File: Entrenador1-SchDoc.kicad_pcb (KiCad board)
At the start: 2 copper layers, 152.4 x 106.7 mm, 88 parts, among them CON1 BARREL_JACK, J11 CON8, J3 ICSP, J5 CON8, J6 CON8, J7 CON8, J9 3vias, P1 CONN_01X04, P10 CONN_01X04, P2 CONN_01X04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

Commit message: adición del BOM
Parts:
- C10, C9: value C -> 22pf
- C11: value CP -> 1uf
- C6: value ~ -> 10uf
- C7: value C -> 100nf
- C8: value CP -> 47uf
- D12: value D -> 1n4004
- RV1, RV2: value POT -> 10K lin
- Y2: value XTAL -> 20MHz
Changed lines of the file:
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@@
   (general
     (links 239)
-    (no_connects 0)
-    (area 65.989999 32.969999 218.490001 139.750001)
+    (no_connects 13)
+    (area 64.616667 32.969999 230.290572 149.258)
     (thickness 1.6)
     (drawings 118)
@@
       (effects (font (size 1 1) (thickness 0.15)))
     )
-    (fp_text value C (at 1.25 2.56) (layer F.Fab)
+    (fp_text value 22pf (at 1.25 2.56) (layer F.Fab)
       (effects (font (size 1 1) (thickness 0.15)))
     )
@@
       (effects (font (size 1 1) (thickness 0.15)))
     )
-    (fp_text value C (at 1.25 2.56 180) (layer F.Fab)
+    (fp_text value 22pf (at 1.25 2.56 180) (layer F.Fab)
       (effects (font (size 1 1) (thickness 0.15)))
     )
@@
       (effects (font (size 1 1) (thickness 0.15)))
     )
-    (fp_text value C (at 1.25 2.56 180) (layer F.Fab)
+    (fp_text value 100nf (at 1.25 2.56 180) (layer F.Fab)
       (effects (font (size 1 1) (thickness 0.15)))
     )
@@
       (effects (font (size 1 1) (thickness 0.15)))
     )
-    (fp_text value CP (at 1.25 3.81 180) (layer F.Fab)
+    (fp_text value 1uf (at 1.25 3.81 180) (layer F.Fab)
       (effects (font (size 1 1) (thickness 0.15)))
     )
@@
       (effects (font (size 1 1) (thickness 0.15)))
     )
-    (fp_text value CP (at 1.25 3.81 270) (layer F.Fab)
+    (fp_text value 47uf (at 1.25 3.81 270) (layer F.Fab)
       (effects (font (size 1 1) (thickness 0.15)))
     )
@@
       (effects (font (size 1 1) (thickness 0.15)))
     )
-    (fp_text value ~ (at 1.25 4.46 90) (layer F.Fab)
+    (fp_text value 10uf (at 1.25 4.46 90) (layer F.Fab)
       (effects (font (size 1 1) (thickness 0.15)))
     )
@@
       (effects (font (size 1 1) (thickness 0.15)))
     )
-    (fp_text value D (at 5.08 2.91) (layer F.Fab)
+    (fp_text value 1n4004 (at 5.08 2.91) (layer F.Fab)
       (effects (font (size 1 1) (thickness 0.15)))
     )
@@
       (effects (font (size 1 1) (thickness 0.15)))
     )
-    (fp_text value POT (at 9.915 4.7) (layer F.Fab)
+    (fp_text value "10K lin" (at 9.915 4.7) (layer F.Fab)
       (effects (font (size 1 1) (thickness 0.15)))
     )
@@
       (effects (font (size 1 1) (thickness 0.15)))
     )
-    (fp_text value POT (at 9.915 4.7) (layer F.Fab)
+    (fp_text value "10K lin" (at 9.915 4.7) (layer F.Fab)
       (effects (font (size 1 1) (thickness 0.15)))
     )
@@
       (effects (font (size 1 1) (thickness 0.15)))
     )
-    (fp_text value XTAL (at 2.44 3.525 180) (layer F.Fab)
+    (fp_text value 20MHz (at 2.44 3.525 180) (layer F.Fab)
       (effects (font (size 1 1) (thickness 0.15)))
     )

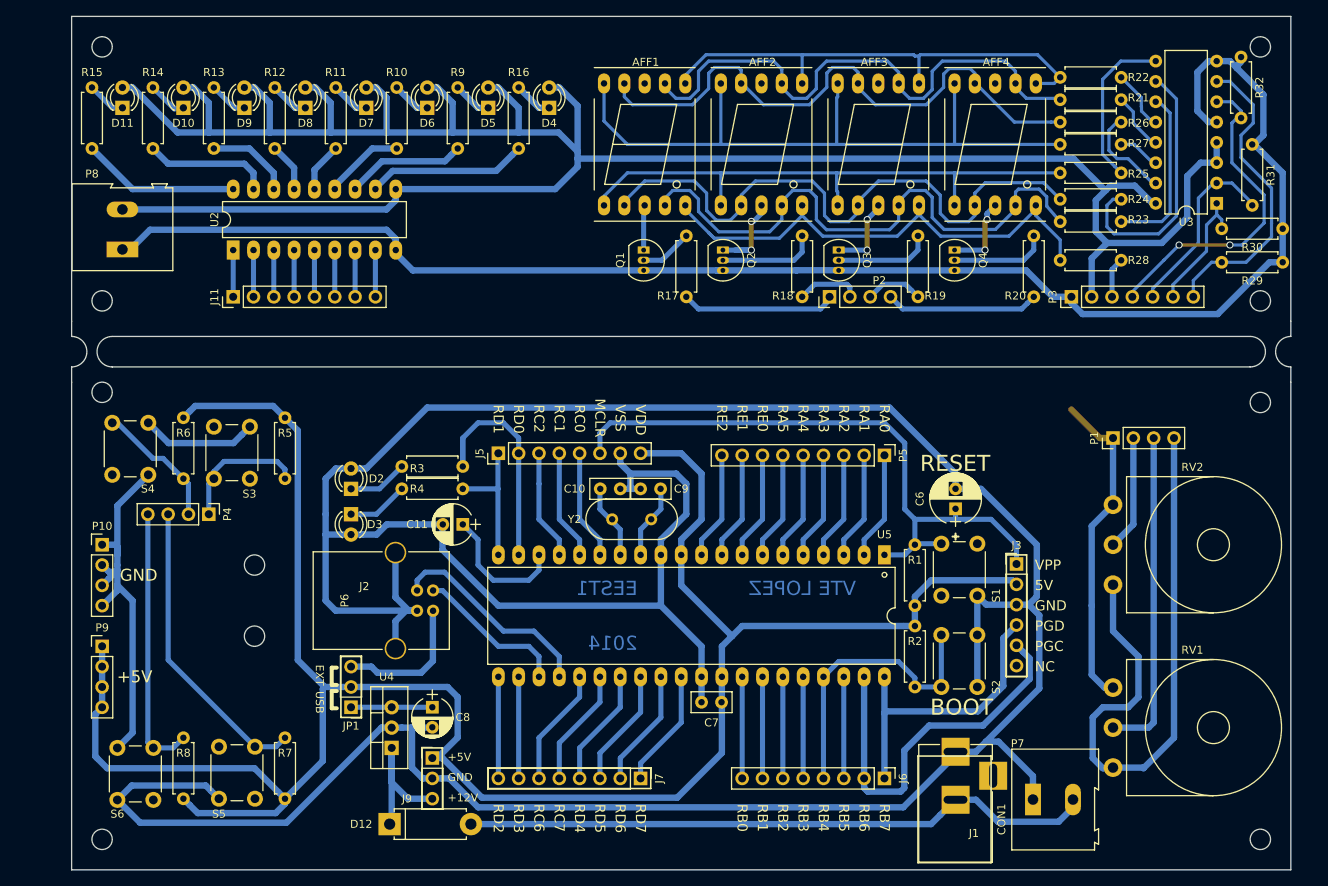
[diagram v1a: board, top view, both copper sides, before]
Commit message: se agrandan PADS
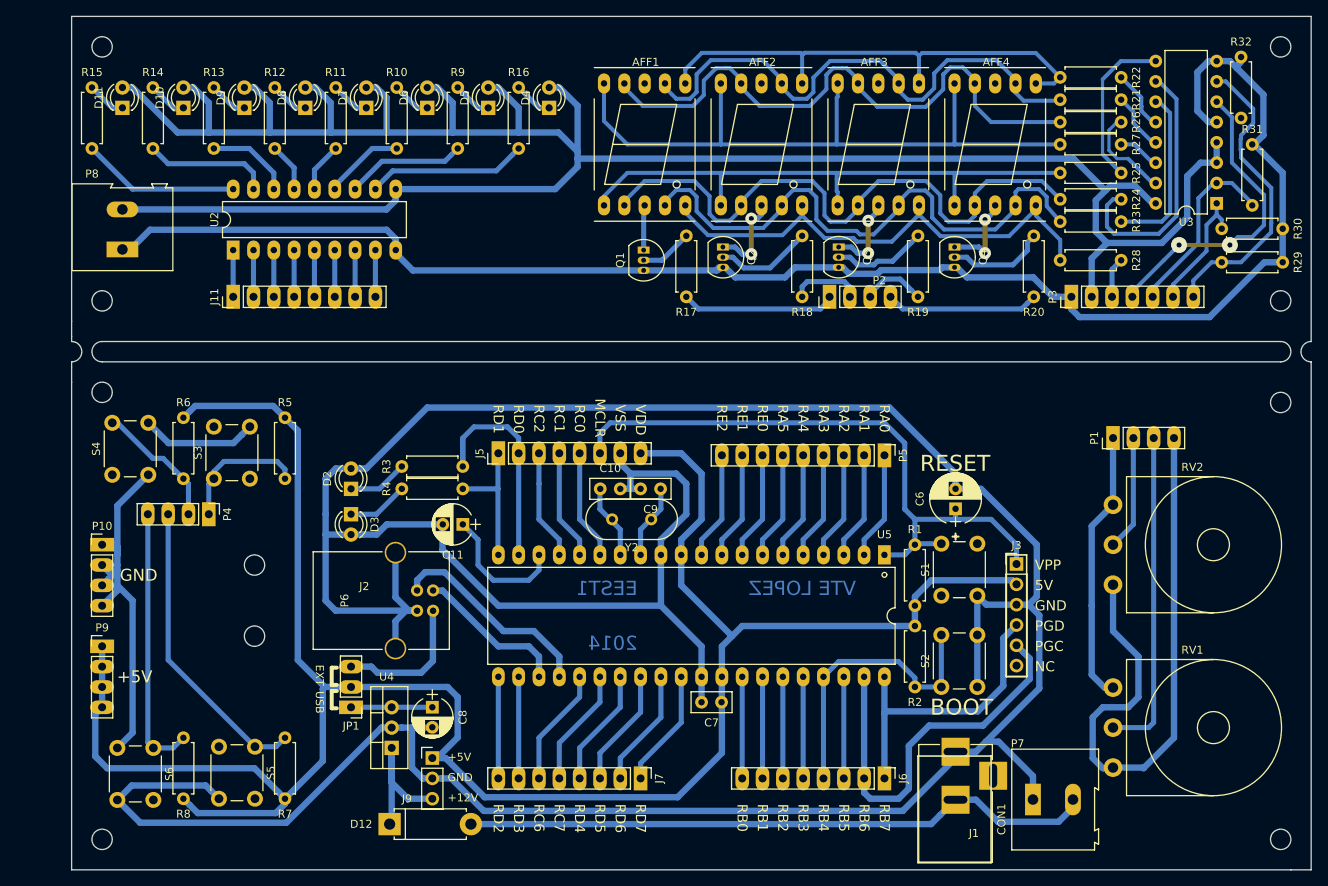
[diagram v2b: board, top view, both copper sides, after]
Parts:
- JP1: footprint libreria:Pin_Header_Straight_1x03_Pitch2.54mm -> Pin_Header_Straight_1x03_Pitch2.54mm
- P2: footprint libreria:Socket_Strip_Straight_1x04_Pitch2.54mm -> Socket_Strip_Straight_1x04_Pitch2.54mm
- P3: footprint libreria:Socket_Strip_Straight_1x07_Pitch2.54mm -> Socket_Strip_Straight_1x07_Pitch2.54mm
- P5: footprint libreria:Socket_Strip_Straight_1x09_Pitch2.54mm -> Socket_Strip_Straight_1x09_Pitch2.54mm
- moved Q2 0.38 mm to (147.4, 61.8)
- moved Q3 0.38 mm to (161.9, 61.8)
- moved Q4 0.38 mm to (176.4, 61.8)
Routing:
- net GND: track 738.4 -> 735.3 mm
- net /Display_D: track 40.5 -> 38.6 mm
- net /c: track 73.6 -> 72.2 mm
- net PGC: track 48.3 -> 49.7 mm
- net /a: track 69.7 -> 68.5 mm
- net Disp2: track 7.97 -> 9.00 mm
- net /b: track 60.7 -> 61.7 mm
- net Net-(AFF3-Pad3): track 9.72 -> 10.5 mm
- net Net-(AFF4-Pad3): track 9.92 -> 10.7 mm
- net Disp3: track 7.27 -> 8.03 mm
- net /Display_A: track 39.1 -> 38.5 mm
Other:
- board size 152.4 x 106.7 mm -> 154.9 x 106.7 mm
- net class display: trace_width 0.4 -> 0.5

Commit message: cambio de huellas transistores, ajuste de pistas según prototipo
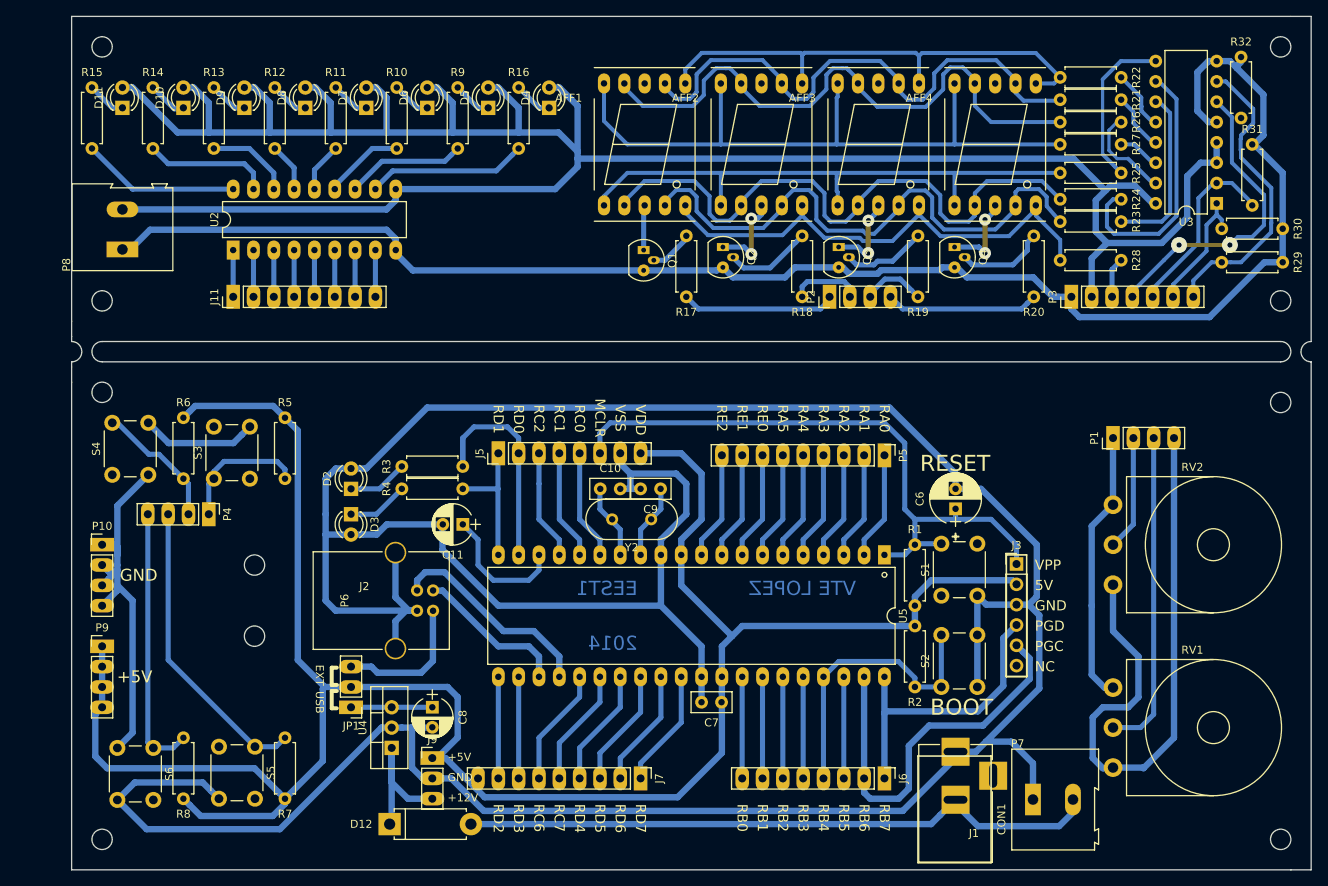
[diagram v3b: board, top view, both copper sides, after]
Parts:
- J7: footprint libreria:Socket_Strip_Straight_1x08_Pitch2.54mm -> libreria:Socket_Strip_Straight_1x09_Pitch2.54mm
- JP1: footprint Pin_Header_Straight_1x03_Pitch2.54mm -> libreria:Pin_Header_Straight_1x03_Pitch2.54mm
- P2: footprint Socket_Strip_Straight_1x04_Pitch2.54mm -> libreria:Socket_Strip_Straight_1x04_Pitch2.54mm
- P3: footprint Socket_Strip_Straight_1x07_Pitch2.54mm -> libreria:Socket_Strip_Straight_1x07_Pitch2.54mm
- P5: footprint Socket_Strip_Straight_1x09_Pitch2.54mm -> libreria:Socket_Strip_Straight_1x09_Pitch2.54mm
- P7: footprint Terminal_Blocks:TerminalBlock_Altech_AK300-2_P5.00mm -> libreria:TerminalBlock_Altech_AK300-2_P5.00mm
- Q1, Q2, Q3, Q4: footprint libreria:TO-92_Inline_Narrow_Oval -> libreria:TO-92_Molded_Narrow
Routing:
- net GND: track 735.3 -> 736.7 mm
- net Net-(Q4-Pad2): track 12.4 -> 11.1 mm
- net Net-(Q3-Pad2): track 11.8 -> 10.5 mm
- net Net-(Q2-Pad2): track 12.1 -> 10.9 mm
- net +12VFuente: track 79.4 -> 80.5 mm
- net Net-(Q1-Pad2): track 6.60 -> 5.55 mm
- net Net-(P1-Pad3): track 40.9 -> 40.3 mm

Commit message: En base al prototipo, se replantean las posiciones de los elementos
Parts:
- removed CON1: BARREL_JACK, libreria:BARREL_JACK
- Q1, Q2, Q3, Q4: footprint libreria:TO-92_Molded_Narrow -> TO_SOT_Packages_THT:TO-92_Molded_Narrow
- R10, R11, R12, R13, R14, R15, R16, R9: value 330 -> 180
- R17, R18, R19, R20: value 470 -> 1200
- R21, R22, R23, R24, R25, R26, R27, R28: value 470 -> 180
- R29, R30, R31, R32: value 1200 -> 10k
- moved P7 9.69 mm to (176.6, 129.5)
- moved JP1 3.86 mm to (100.3, 115.6), turned to 90 degrees
- moved U4 1.27 mm to (106.0, 125.7)
- moved C11 1.23 mm to (114.9, 97.8), turned to 90 degrees
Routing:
- net GND: track 736.7 -> 767.2 mm
- net +12VFuente: track 80.5 -> 68.1 mm
- net VUR: track 19.9 -> 9.33 mm
- net VDD: track 568.2 -> 576.0 mm
- net +5VUSB: track 17.5 -> 12.9 mm
- net Net-(C8-Pad1): track 10.2 -> 13.8 mm
- net Net-(C11-Pad1): track 16.7 -> 13.3 mm
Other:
- board text removed: "EXT"
- board text removed: "USB"

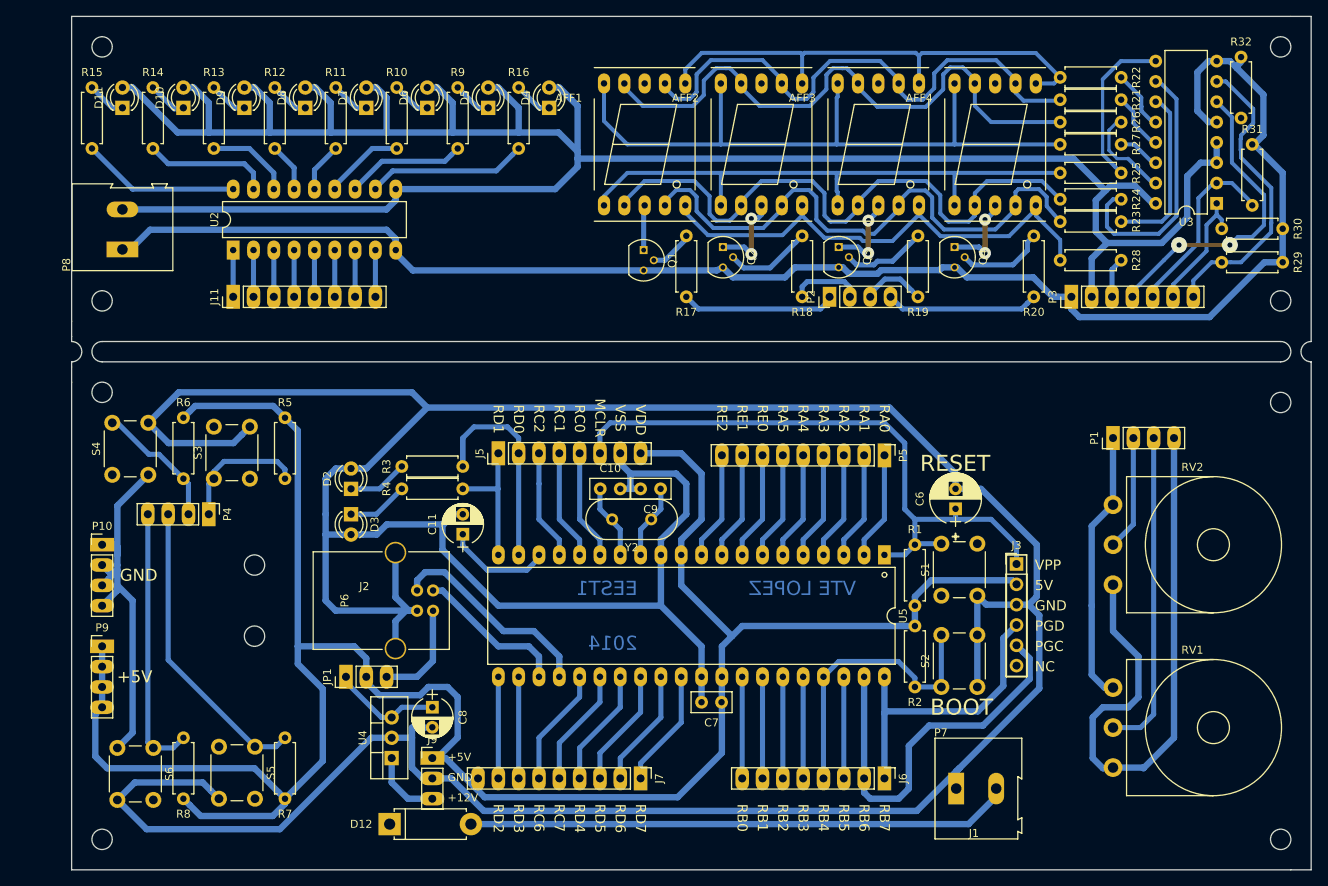
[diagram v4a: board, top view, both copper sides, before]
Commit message: Se agrega un diodo de protección a la placa de visualización Se eliminan los pines extra de alimentación de la placa de visualización
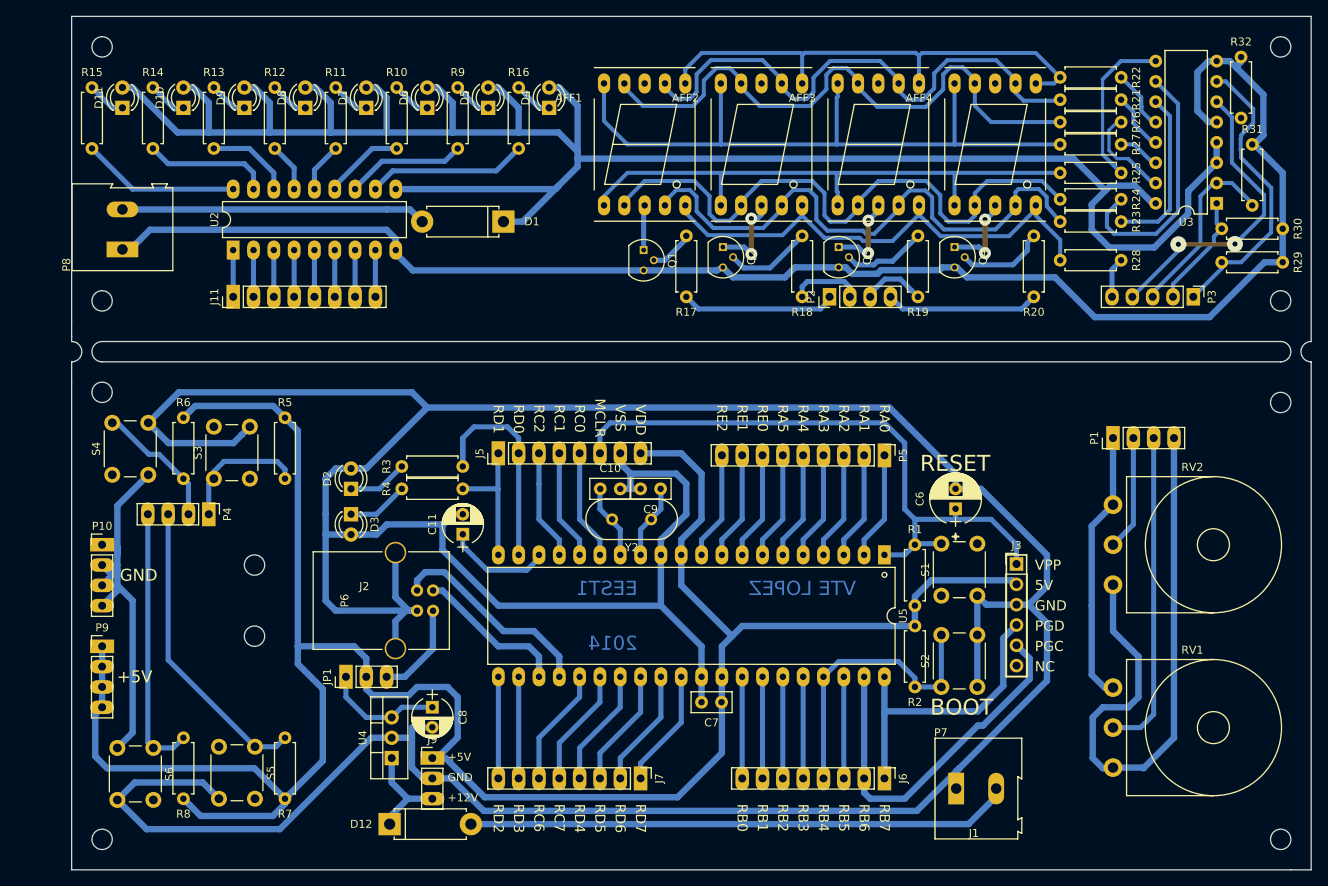
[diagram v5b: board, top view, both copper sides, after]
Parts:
- added D1: 1n4004, libreria:D_5W_P10.16mm_Horizontal, F.Cu at (120.0, 58.7)
- J7: footprint libreria:Socket_Strip_Straight_1x09_Pitch2.54mm -> libreria:Socket_Strip_Straight_1x08_Pitch2.54mm
- P3: value CONN_01X07 -> CONN_01X05; footprint libreria:Socket_Strip_Straight_1x07_Pitch2.54mm -> libreria:Socket_Strip_Straight_1x05_Pitch2.54mm
- moved P3 15.2 mm to (206.2, 68.1), turned to 270 degrees
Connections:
- P1 pad 1: GND -> -VrefAnalogica
- P3 pad 1: GND -> /Display_A
- P3 pad 2: VDD -> /Display_B
- P3 pad 3: /DisplayH -> /Display_C
- P3 pad 5: /Display_C -> /DisplayH
- P8 pad 2: VDD -> Net-(D1-Pad2)
- RV1 pad 3: GND -> -VrefAnalogica
- RV2 pad 3: GND -> -VrefAnalogica
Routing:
- net Net-(D1-Pad2): track 0.00 -> 38.1 mm
- net VDD: track 576.0 -> 541.3 mm
- net -VrefAnalogica: track 0.00 -> 34.0 mm
- net GND: track 767.2 -> 734.1 mm
- net VUR: track 9.33 -> 13.5 mm
- net PGC: track 49.7 -> 46.6 mm
- net /Display_B: track 16.0 -> 14.5 mm
- net Net-(C8-Pad1): track 13.8 -> 14.9 mm
- net +5VUSB: track 12.9 -> 12.0 mm
- net Net-(R24-Pad1): track 32.9 -> 32.0 mm
- net /Display_A: track 38.5 -> 37.7 mm
- net /Display_D: track 38.6 -> 38.0 mm
- net Net-(R23-Pad1): track 21.5 -> 20.9 mm
